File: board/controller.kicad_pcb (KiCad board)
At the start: 2 copper layers, 157 x 120.5 mm, 145 parts, among them IC101 ATMEGA8A-P, IC301 MCP2551-I/P, J301 DB9, P101 CONN_4, P102 CONN_8, P201 CONN_14, P202 CONN_14, P203 MICROSD, P301 CONN_2X2, Q101 PNP, Q102 PNP, Q103 NPN, Q104 NPN, Q105 NPN, Q106 PNP, Q107 PNP, Q108 MOSFET_N, Q109 MOSFET_N, Q201 MOSFET_P, SW201 SWITCH_PUSH, SW202 SWITCH_PUSH, SW203 SWITCH_PUSH, U101 LM393, U102 7805, U201 LM6206N3-3.3, U202 LSF0108, U203 4066, U301 MCP2515-I/P, X101 8MHz

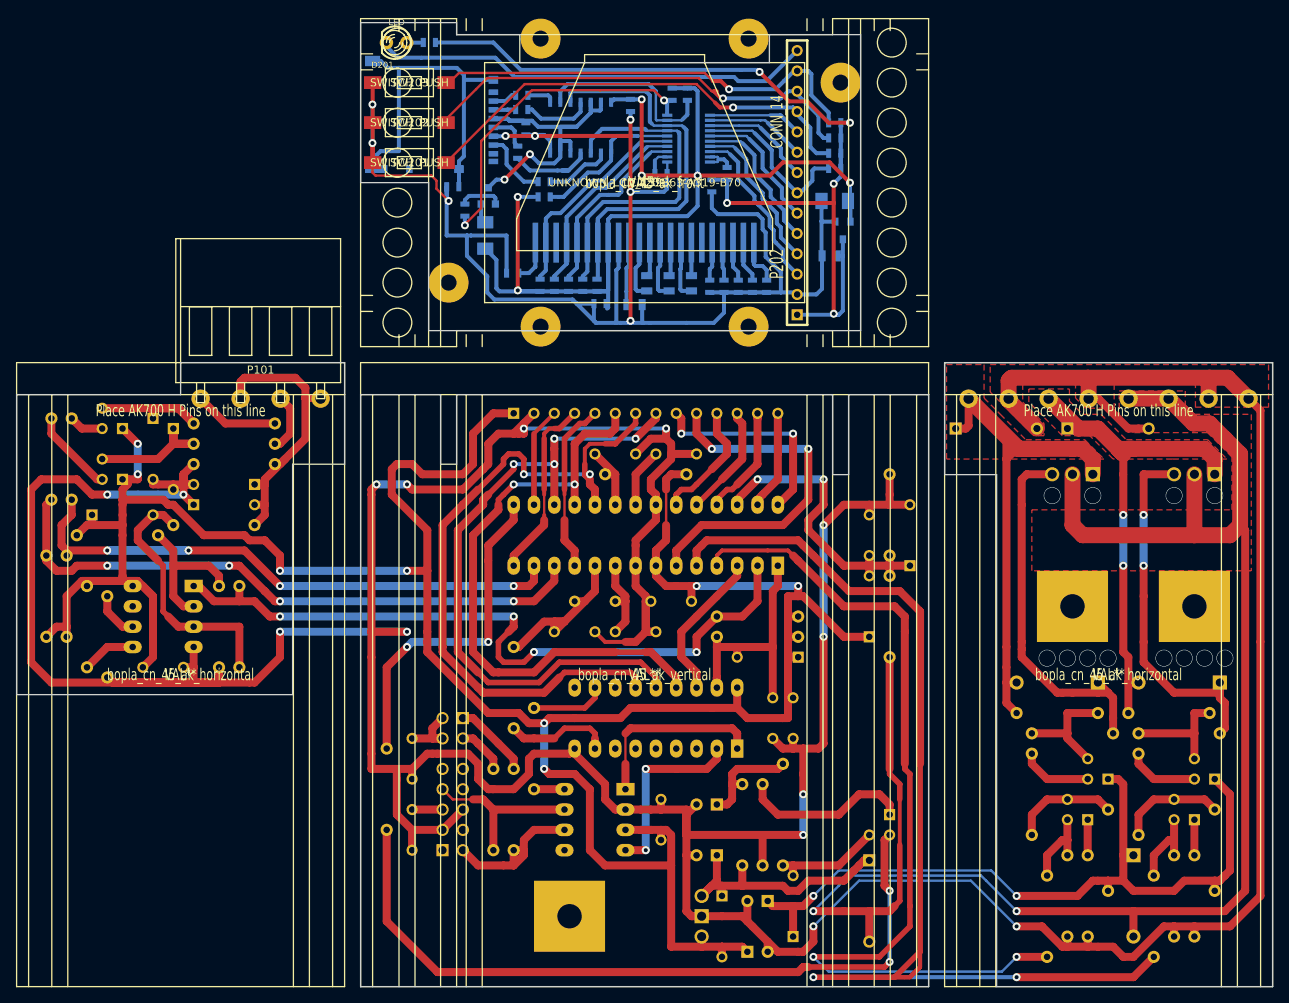
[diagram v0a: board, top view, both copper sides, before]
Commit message: Fix nterchanges RESET and CS pin of display
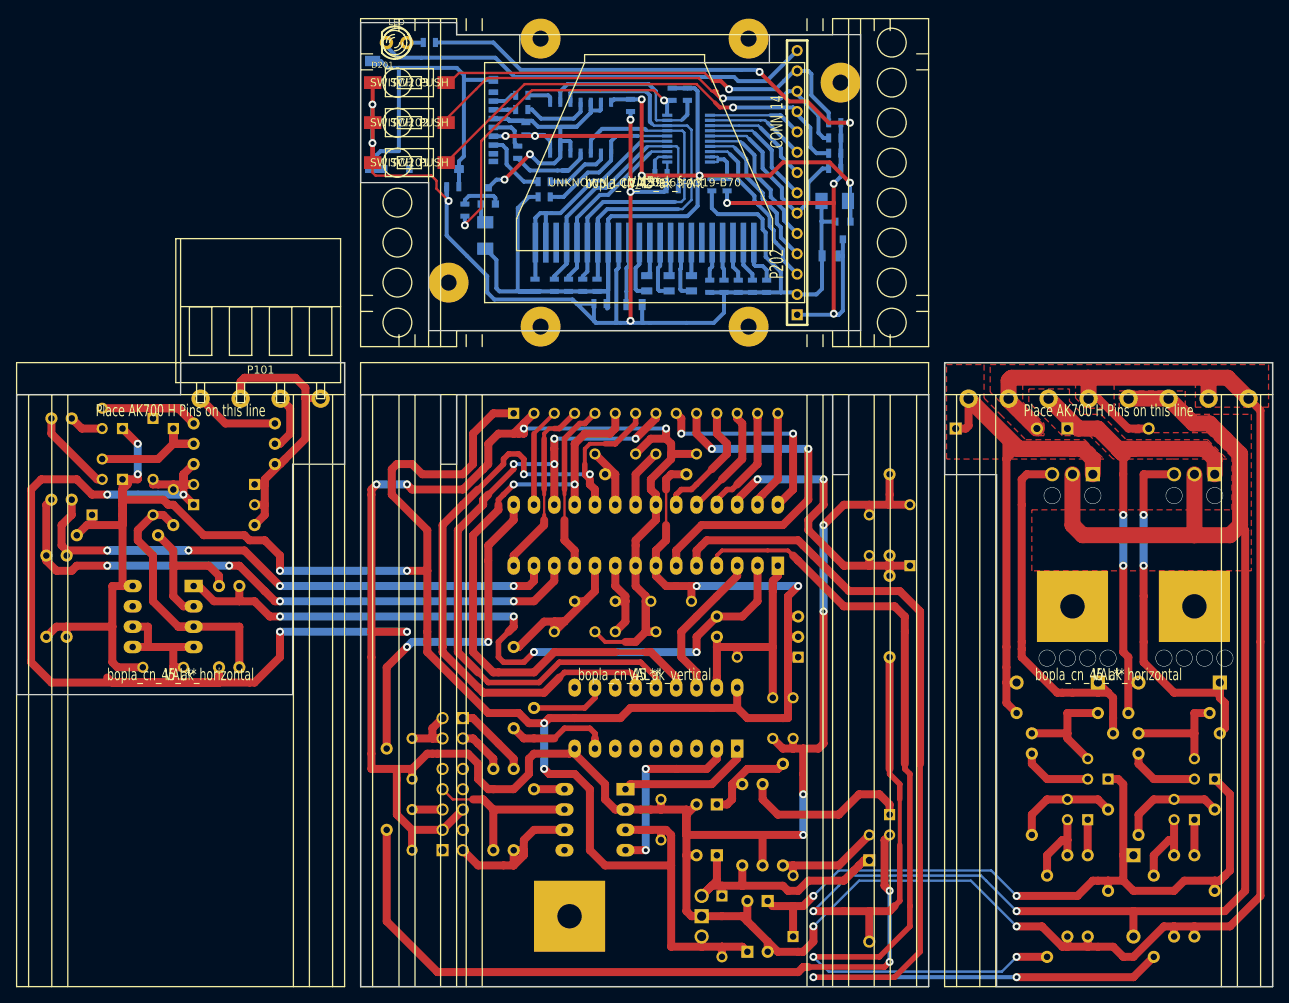
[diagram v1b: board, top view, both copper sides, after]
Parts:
- removed D107: DIODE, D3
- removed R116, R117: 10k, R4
- D108: value DIODE -> 4V7
- moved C213 22.6 mm to (147.4, 48.8), turned to 180 degrees
- moved R208 1.40 mm to (154.3, 48.3)
- moved R217 0.64 mm to (130.3, 60.8)
- moved C203 0.13 mm to (152.4, 48.3)
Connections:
- C202 pad 1: N-00000140 (its old number) -> N-00000143
- C203 pad 1: N-00000140 (its old number) -> N-00000119
- C213 pad 1: GND -> N-00000102
- C213 pad 2: N-00000104 (its old number) -> GND
- IC101 pad 11: /Display/RESET_LCD -> /Display/CS_LCD
- IC101 pad 14: /Display/CS_LCD -> /Display/RESET_LCD
- LCD201 pad 1: N-00000104 (its old number) -> N-00000113
- LCD201 pad 2: N-00000118 (its old number) -> N-00000113
- LCD201 pad 4: N-00000105 (its old number) -> N-00000102
- P201 pad 4: /Display/CS_LCD -> /Display/RESET_LCD
- P201 pad 5: /Display/RESET_LCD -> /Display/CS_LCD
- P202 pad 1: N-00000140 (its old number) -> N-00000143
- P202 pad 6: N-00000147 -> N-00000142
- P202 pad 7: N-00000146 -> N-00000141
- R201 pad 2: N-00000140 (its old number) -> N-00000143
- R202 pad 2: N-00000140 (its old number) -> N-00000143
- R203 pad 2: N-00000140 (its old number) -> N-00000143
- R204 pad 2: N-00000140 (its old number) -> N-00000143
- R206 pad 1: N-00000146 -> N-00000142
- R206 pad 2: N-00000140 (its old number) -> N-00000143
- R208 pad 1: N-00000140 (its old number) -> N-00000143
- R208 pad 2: N-00000135 (its old number) -> N-00000119
- R217 pad 2: N-00000118 (its old number) -> N-00000113
- R221 pad 2: N-00000105 (its old number) -> N-00000102
- U101 pad 5: N-0000035 -> GND
- U101 pad 6: N-0000036 -> GND
- U201 pad 3: N-00000140 (its old number) -> N-00000143
- U202 pad 14: N-00000146 -> N-00000141
- U202 pad 15: N-00000147 -> N-00000142
- U202 pad 19: N-00000135 (its old number) -> N-00000119
- U202 pad 20: N-00000135 (its old number) -> N-00000119
- U202 pad 4: N-00000105 (its old number) -> N-00000102
- U202 pad 5: N-00000118 (its old number) -> N-00000113
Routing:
- net N-00000140 (its old number): track 117.1 -> 0.00 mm, vias 5 -> 0
- net N-00000143: track 0.00 -> 113.8 mm, vias 0 -> 5
- net /Echa: track 225.5 -> 149.0 mm
- net N-00000113: track 0.00 -> 31.9 mm
- net N-00000102: track 0.00 -> 31.2 mm
- net N-00000118 (its old number): track 27.1 -> 0.00 mm
- net N-00000142: track 0.00 -> 26.3 mm
- net N-00000105 (its old number): track 24.6 -> 0.00 mm
- net N-0000081: track 38.9 -> 16.8 mm
- net N-00000146: track 21.3 -> 0.00 mm
- net N-00000147: track 18.6 -> 0.00 mm
- net +5V: track 355.6 -> 337.7 mm
- net N-00000141: track 0.00 -> 15.4 mm
- net N-00000119: track 0.00 -> 8.96 mm
- net N-0000035: track 6.77 -> 0.00 mm
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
